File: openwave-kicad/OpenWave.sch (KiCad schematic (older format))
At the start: 42 parts, among them IC1 STM32F405RGT, J1 USB_OTG, J2 503182-1852, SW1 SW_Push, Y1 8MHz, Y2 32.768KHz

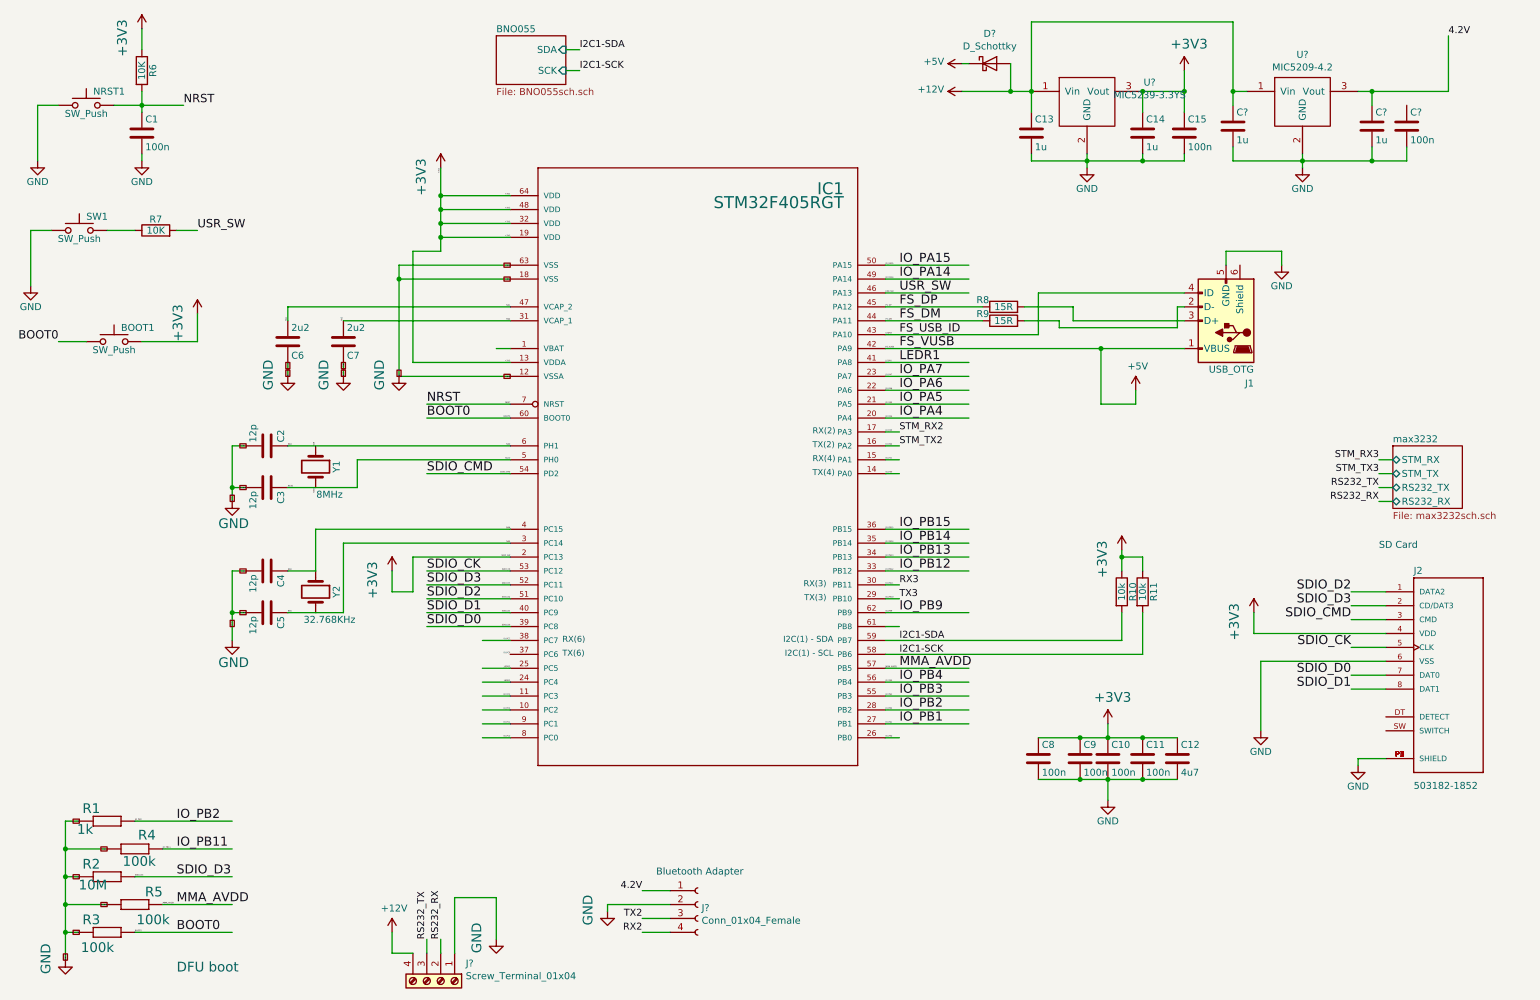
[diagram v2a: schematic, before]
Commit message: linked all footprints to symbols, ready for routing
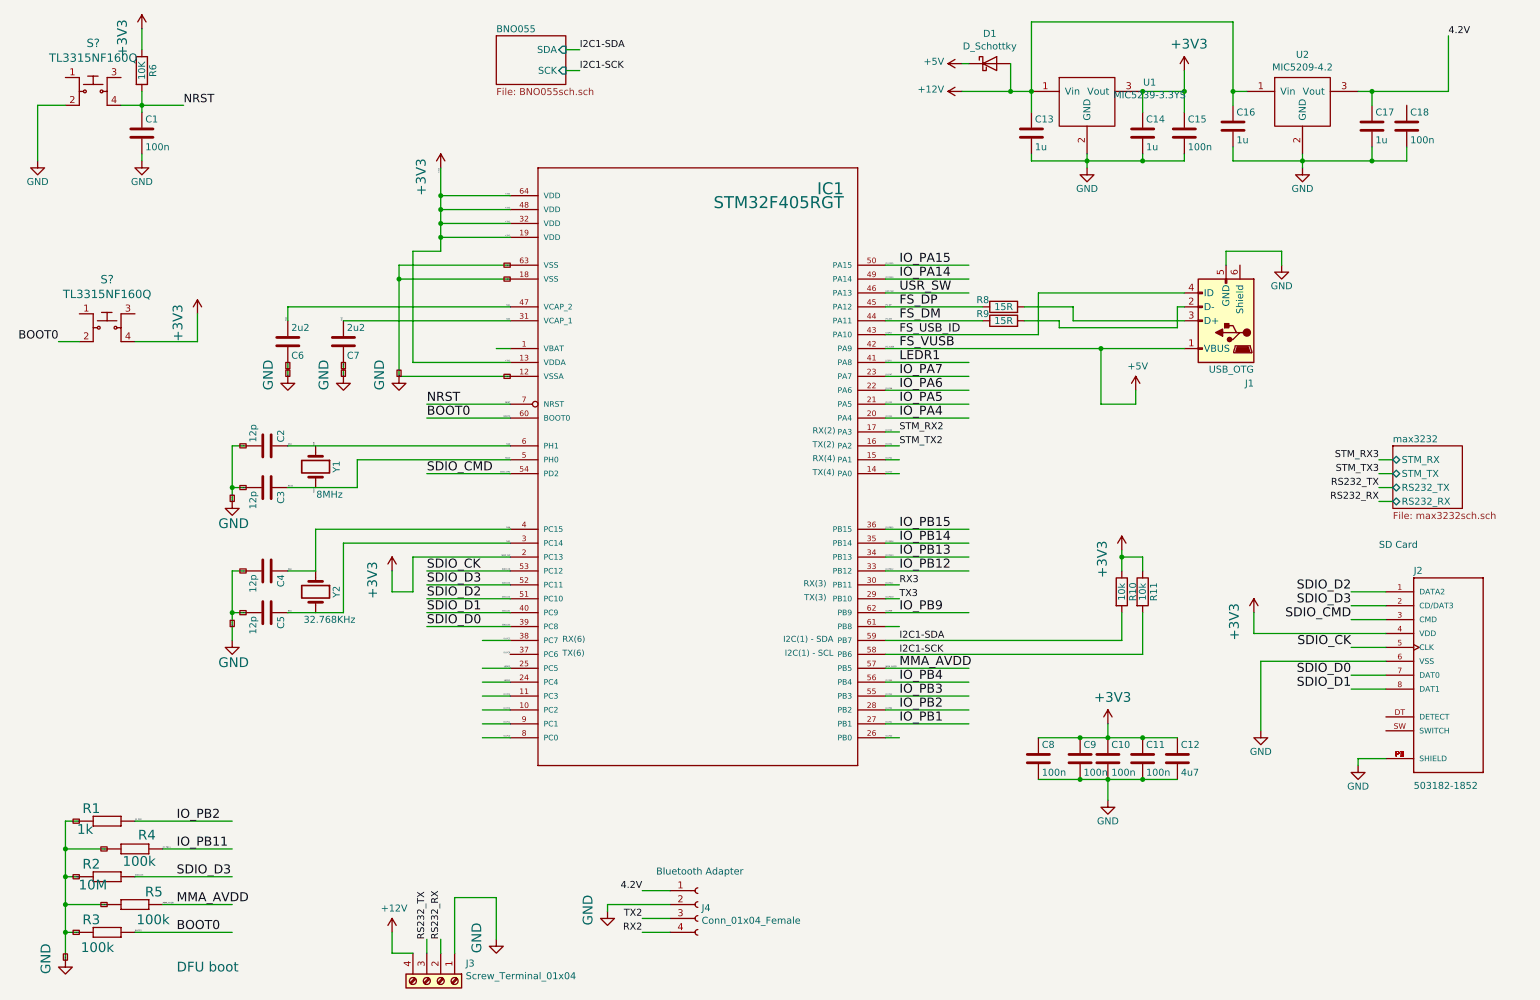
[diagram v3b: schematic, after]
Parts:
- removed BOOT1, NRST1, SW1: SW_Push, symbol Switch:SW_Push
- removed R7: 10K, Resistors_SMD:R_0603, symbol Device:R
- added S? (x2): TL3315NF160Q, digikey-footprints:Switch_Tactile_SMD_4.5x4.5mm_TL3315NF160Q, symbol dk_Tactile-Switches:TL3315NF160Q
- C1, C10, C11, C12, C13, C14, C15, C2, C3, C4, C5, C6, C7, C8, C9: footprint Capacitors_SMD:C_0603 -> Capacitor_SMD:C_0603_1608Metric
- C16, C17, C18: renamed from C?; footprint Capacitors_SMD:C_0603 -> Capacitor_SMD:C_0603_1608Metric
- D1: renamed from D?; footprint (none) -> Diode_SMD:D_0201_0603Metric
- J1: footprint (none) -> my_footprints:USB_Micro-B_Molex-105017-0001
- J3: renamed from J?; footprint (none) -> my_footprints:4-WAY-PCB_SOCKET
- J4: renamed from J?; footprint (none) -> Connector_PinHeader_2.54mm:PinHeader_1x04_P2.54mm_Vertical
- R1, R10, R11, R2, R3, R4, R5, R6, R8, R9: footprint Resistors_SMD:R_0603 -> Resistor_SMD:R_0603_1608Metric
- U1, U2: renamed from U?; footprint (none) -> Package_TO_SOT_SMD:SOT-223-3_TabPin2
- Y1: footprint minibuoy:QC5CA8_8mhz_oscillator -> my_footprints:QC5CA8_8mhz_oscillator
- Y2: footprint minibuoy:ABS06-32.768KHZ_smd_crystal -> my_footprints:ABS06-32.768KHZ_smd_crystal
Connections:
- wire segments 219 -> 215

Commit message: fixed unconnected nets, routing 15% done
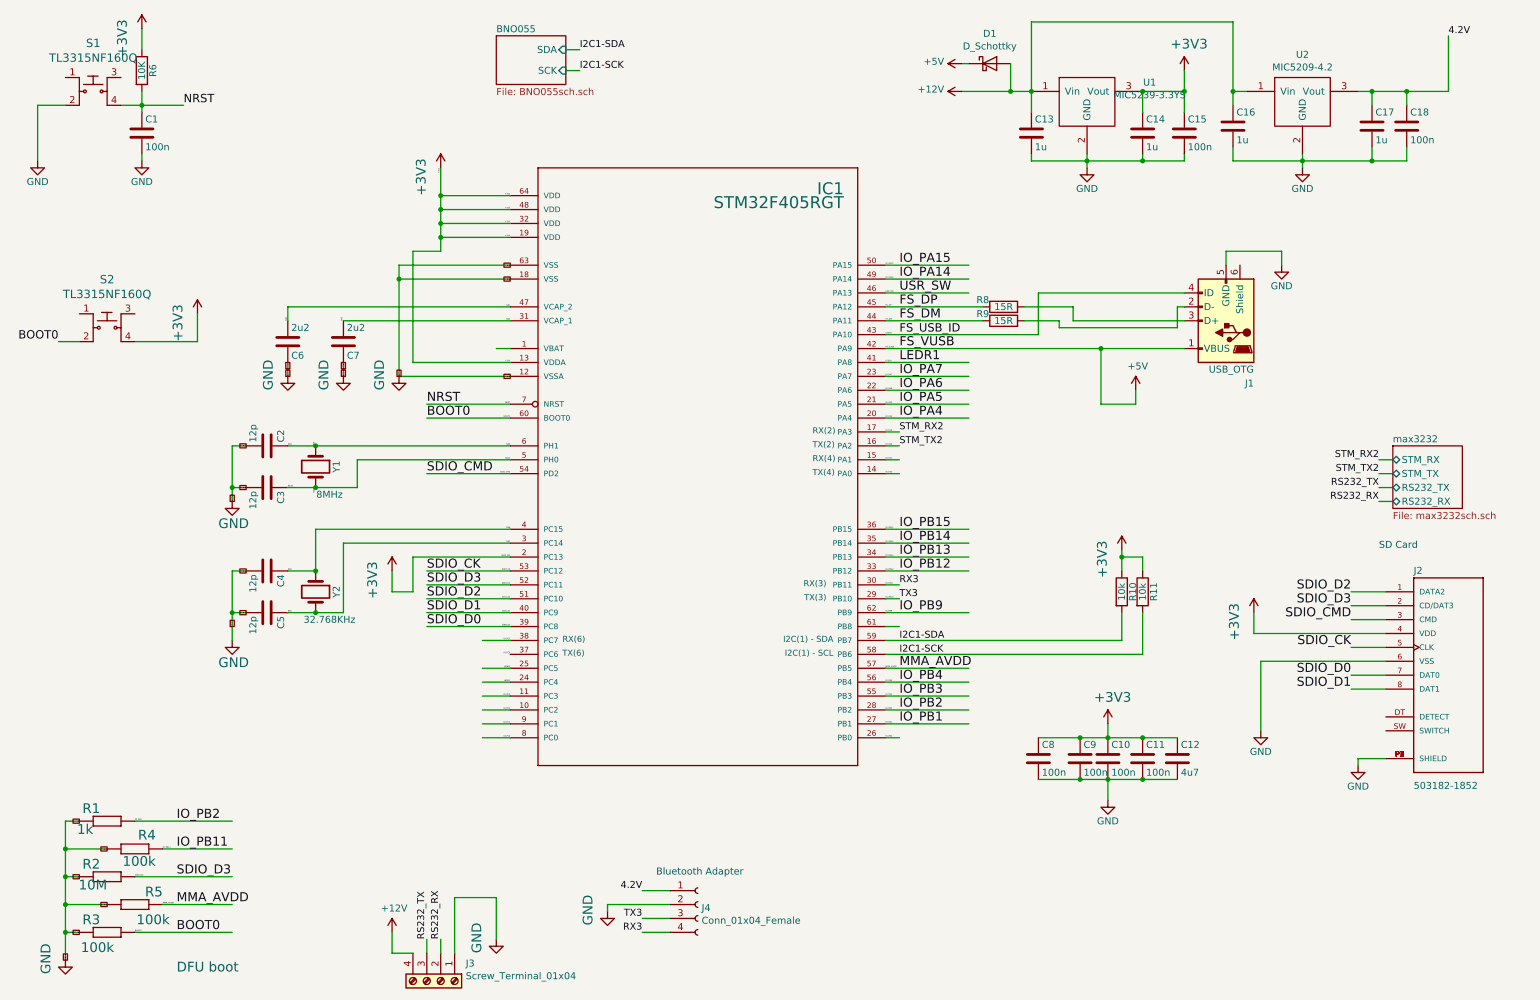
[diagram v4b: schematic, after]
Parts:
- gave numbers to parts that had none: 2
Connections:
- net labels removed: RX2, STM_RX3, STM_TX3, TX2
- wire segments 215 -> 220
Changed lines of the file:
@@
 	2800 4350 2800 4850
-Wire Wire Line
-	4000 4250 2600 4250
 Wire Wire Line
 	4000 3750 2900 3750
@@
 	2400 4550 2600 4550
 Wire Wire Line
-	2600 4550 2600 4250
-Wire Wire Line
 	8400 5050 8400 4850
 Wire Wire Line
@@
 	2000 4850 2000 5050
 Wire Wire Line
-	2400 3650 4000 3650
-Wire Wire Line
-	2400 3950 2900 3950
-Wire Wire Line
 	7800 5750 8100 5750
 Wire Wire Line
 	7800 6050 8100 6050
-Wire Wire Line
-	2400 4850 2800 4850
 Wire Wire Line
 	8300 6050 8550 6050
@@
 Connection ~ 10200 1100
 Wire Wire Line
-	10200 1100 10750 1100
+	10200 1100 10450 1100
 Wire Wire Line
 	10200 1500 10200 1600
@@
 STM_TX2
 Text Label 4950 7150 2    50   ~ 0
-RX2
+RX3
 Text Label 4950 7050 2    50   ~ 0
-TX2
+TX3
 Wire Wire Line
 	4950 7050 5150 7050
@@
 	10350 3850 10250 3850
 Text Label 10250 3750 2    50   ~ 0
-STM_RX3
+STM_RX2
 Text Label 10250 3850 2    50   ~ 0
-STM_TX3
+STM_TX2
 $Sheet
 S 10350 3650 500  450
@@
 	4400 950  4500 950
 $Comp
-L dk_Tactile-Switches:TL3315NF160Q S?
+L dk_Tactile-Switches:TL3315NF160Q S1
 U 1 1 5CAE2BA4
 P 1000 1100
-F 0 "S?" H 1000 1447 60  0000 C CNN
+F 0 "S1" H 1000 1447 60  0000 C CNN
 F 1 "TL3315NF160Q" H 1000 1341 60  0000 C CNN
 F 2 "digikey-footprints:Switch_Tactile_SMD_4.5x4.5mm_TL3315NF160Q" H 1200 1300 60  0001 L CNN
@@
 	1200 1200 1350 1200
 $Comp
-L dk_Tactile-Switches:TL3315NF160Q S?
+L dk_Tactile-Switches:TL3315NF160Q S2
 U 1 1 5CAFC64D
 P 1100 2800
-F 0 "S?" H 1100 3147 60  0000 C CNN
+F 0 "S2" H 1100 3147 60  0000 C CNN
 F 1 "TL3315NF160Q" H 1100 3041 60  0000 C CNN
 F 2 "digikey-footprints:Switch_Tactile_SMD_4.5x4.5mm_TL3315NF160Q" H 1300 3000 60  0001 L CNN
@@
 Wire Wire Line
 	1300 2900 1750 2900
+Wire Wire Line
+	2600 4550 2600 4250
+Wire Wire Line
+	2600 4250 4000 4250
+Connection ~ 2600 4550
+Wire Wire Line
+	2400 4850 2600 4850
+Wire Wire Line
+	2600 4850 2800 4850
+Connection ~ 2600 4850
+Wire Wire Line
+	2400 3650 2600 3650
+Wire Wire Line
+	4000 3650 2600 3650
+Connection ~ 2600 3650
+Wire Wire Line
+	2400 3950 2600 3950
+Wire Wire Line
+	2900 3950 2600 3950
+Connection ~ 2600 3950
+Wire Wire Line
+	10450 1200 10450 1100
+Connection ~ 10450 1100
+Wire Wire Line
+	10450 1100 10750 1100
 $EndSCHEMATC

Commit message: routing ...51 connections left
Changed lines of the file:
@@
 	4000 4750 3400 4750
-Wire Wire Line
-	4000 4650 3400 4650
 Wire Wire Line
 	1300 6750 2000 6750
@@
 Wire Wire Line
 	10450 1100 10750 1100
+Wire Wire Line
+	3400 4650 4000 4650
 $EndSCHEMATC

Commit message: routing finished
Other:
- note added: "BT_GND"
- note added: "BT_RX"
- note added: "BT_TX"
- note added: "BT_VCC"
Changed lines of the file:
@@
 U 1 1 5CA9DB26
 P 5350 6950
-F 0 "J4" H 5377 6926 50  0000 L CNN
-F 1 "Conn_01x04_Female" H 5377 6835 50  0000 L CNN
+F 0 "J4" H 5300 6550 50  0000 L CNN
+F 1 "Conn_01x04_Female" H 4950 6650 50  0000 L CNN
 F 2 "Connector_PinHeader_2.54mm:PinHeader_1x04_P2.54mm_Vertical" H 5350 6950 50  0001 C CNN
 F 3 "~" H 5350 6950 50  0001 C CNN
@@
 STM_TX2
 Text Label 4950 7150 2    50   ~ 0
+TX3
+Text Label 4950 7050 2    50   ~ 0
 RX3
-Text Label 4950 7050 2    50   ~ 0
-TX3
 Wire Wire Line
 	4950 7050 5150 7050
@@
 Wire Wire Line
 	3400 4650 4000 4650
+Text Notes 5400 7150 0    50   ~ 0
+BT_RX
+Text Notes 5400 7050 0    50   ~ 0
+BT_TX
+Text Notes 5400 6850 0    50   ~ 0
+BT_VCC
+Text Notes 5400 6950 0    50   ~ 0
+BT_GND
 $EndSCHEMATC

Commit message: replaced incorrect usb connector
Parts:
- J1: footprint my_footprints:USB_Micro-B_Molex-105017-0001 -> my_footprints:wurth_usb_connector
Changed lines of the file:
@@
 F 0 "J1" H 8950 3200 50  0000 L CNN
 F 1 "USB_OTG" H 8950 3100 50  0000 L CNN
-F 2 "my_footprints:USB_Micro-B_Molex-105017-0001" H 9300 2700 50  0001 C CNN
+F 2 "my_footprints:wurth_usb_connector" H 9300 2700 50  0001 C CNN
 F 3 "" H 9300 2700 50  0001 C CNN
 	1    9150 2750
